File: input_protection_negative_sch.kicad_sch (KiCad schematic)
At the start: 26 parts, among them Q3 SQJQ160E, Q4 SQJQ160E, U2 LM5067

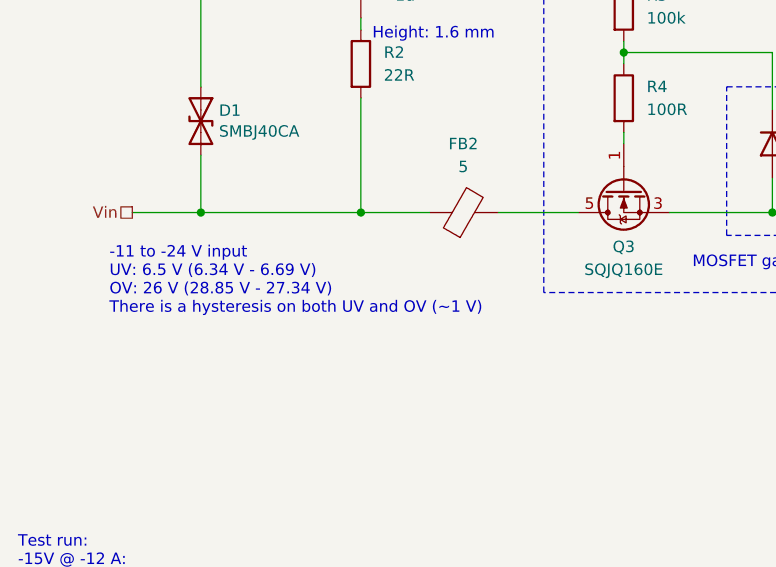
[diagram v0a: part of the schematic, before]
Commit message: Reduced datasheet absolute maximum voltage to ±48 V, because the TVS diodes start conducting considerably at 48 V
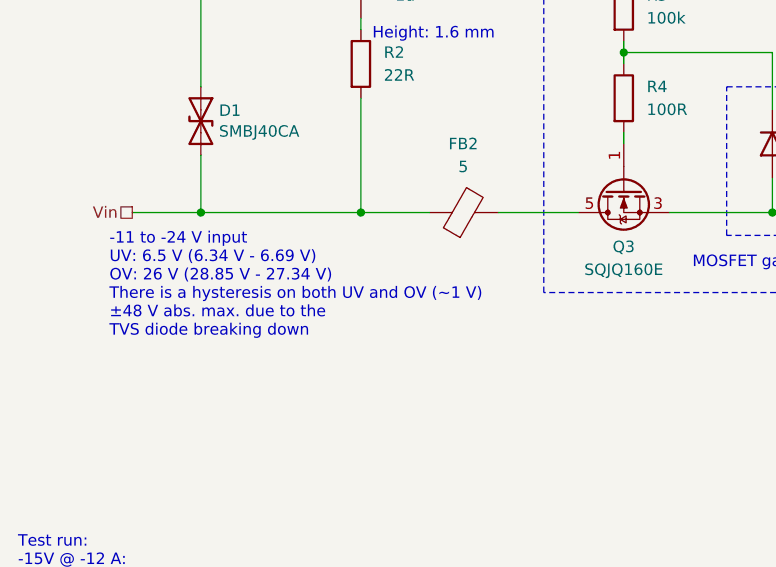
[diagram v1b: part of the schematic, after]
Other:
- note added: "-11 to -24 V input UV: 6.5 V (6.34 V - 6.69 V) OV: 26 V (28.85 V - 27.34 V) There is a hysteresis on both UV and OV (~1 V) ±48 V abs. max. due to the TVS diode breaking down"
- note removed: "-11 to -24 V input UV: 6.5 V (6.34 V - 6.69 V) OV: 26 V (28.85 V - 27.34 V) There is a hysteresis on both UV and OV (~1 V)"
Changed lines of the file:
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@@
     (effects (font (size 1.27 1.27)) (justify left bottom))
   )
-  (text "-11 to -24 V input\nUV: 6.5 V (6.34 V - 6.69 V)\nOV: 26 V (28.85 V - 27.34 V)\nThere is a hysteresis on both UV and OV (~1 V)"
-    (at 36.83 118.11 0)
+  (text "-11 to -24 V input\nUV: 6.5 V (6.34 V - 6.69 V)\nOV: 26 V (28.85 V - 27.34 V)\nThere is a hysteresis on both UV and OV (~1 V)\n±48 V abs. max. due to the\nTVS diode breaking down"
+    (at 36.83 120.65 0)
     (effects (font (size 1.27 1.27)) (justify left bottom))
   )

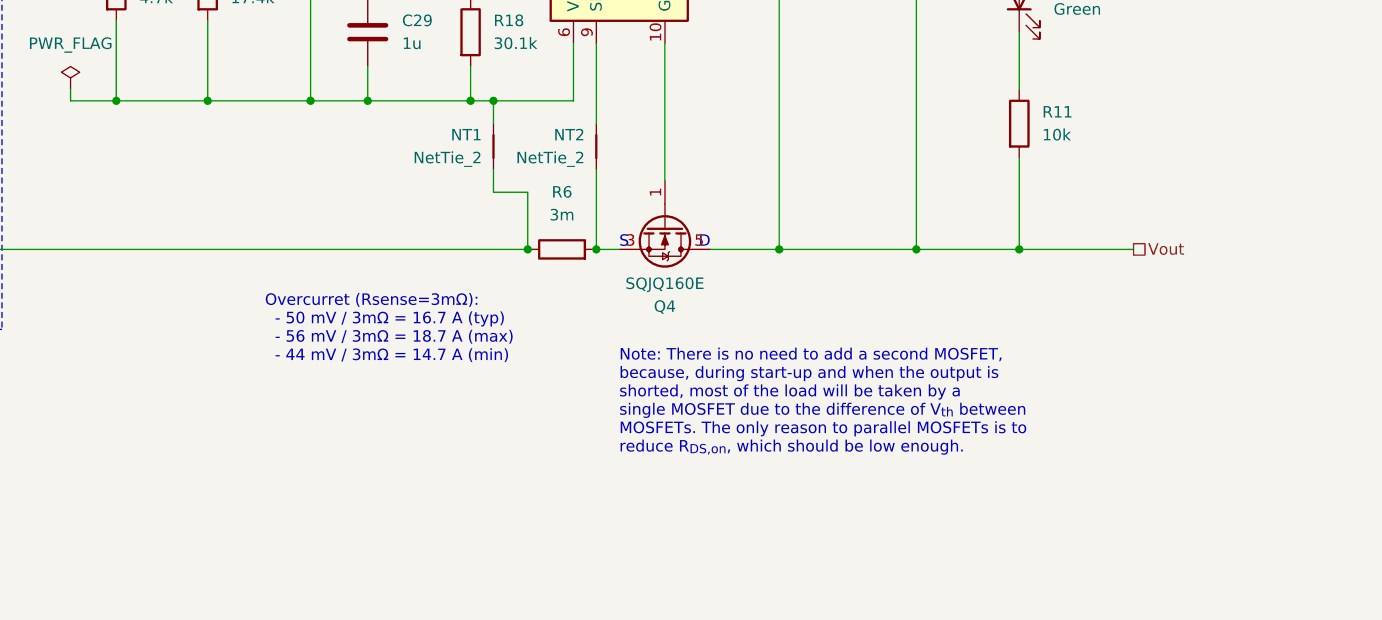
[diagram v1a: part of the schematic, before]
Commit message: Added thermal jumpers Increased copper area at the PMOS and the current sense resistors
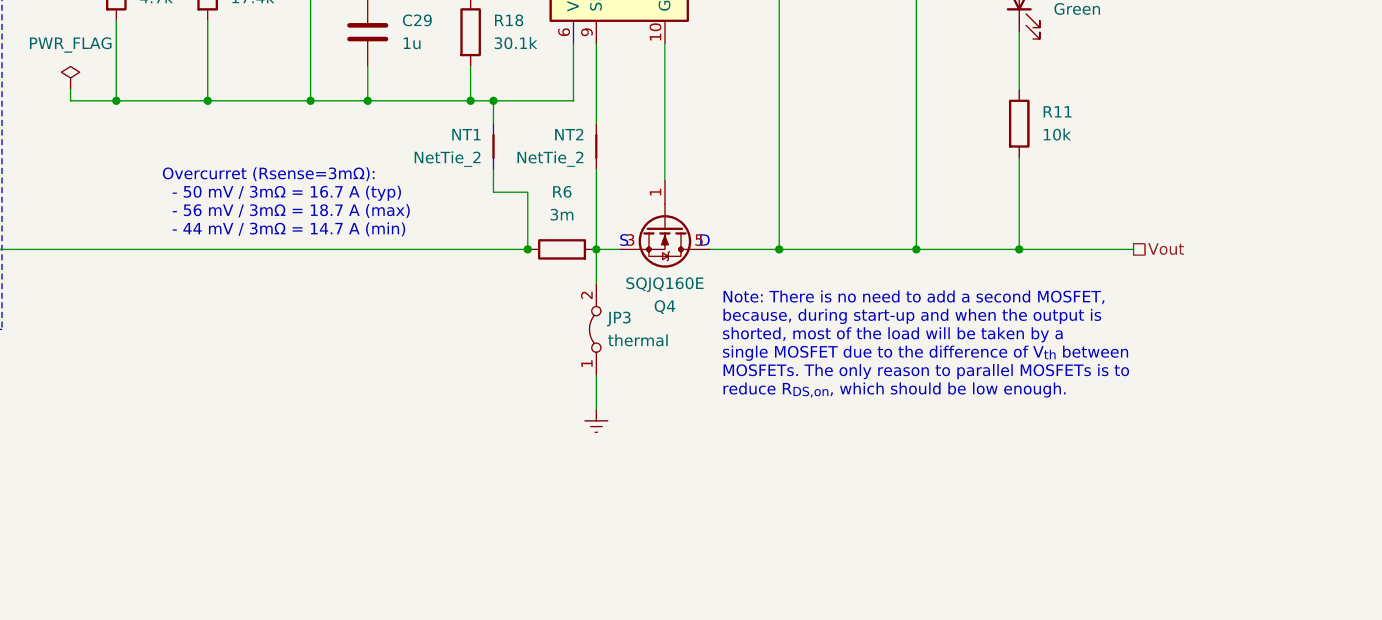
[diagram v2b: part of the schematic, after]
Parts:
- added JP3: thermal, Resistor_SMD:R_0612_1632Metric, symbol Jumper:Jumper_2_Bridged
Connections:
- net at NT2.1, Q4.2 (S), Q4.3 (S)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: now also JP3.2 (B)
- new net Earth: JP3.1 (A)
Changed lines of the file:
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@@
+    (stroke (width 0) (type default))
+  )
+  (wire (pts (xy 205.74 106.68) (xy 205.74 110.49))
     (stroke (width 0) (type default))
   )
@@
   )
   (wire (pts (xy 128.27 39.37) (xy 128.27 85.09))
+    (stroke (width 0) (type default))
+  )
+  (wire (pts (xy 205.74 124.46) (xy 205.74 120.65))
     (stroke (width 0) (type default))
   )
@@
   )
   (text "Note: There is no need to add a second MOSFET,\nbecause, during start-up and when the output is\nshorted, most of the load will be taken by a\nsingle MOSFET due to the difference of V_{th} between\nMOSFETs. The only reason to parallel MOSFETs is to\nreduce R_{DS,on}, which should be low enough."
-    (at 208.28 129.54 0)
+    (at 219.71 123.19 0)
     (effects (font (size 1.27 1.27)) (justify left bottom))
   )
@@
   )
   (text "Overcurret (Rsense=3mΩ):\n  - 50 mV / 3mΩ = 16.7 A (typ)\n  - 56 mV / 3mΩ = 18.7 A (max)\n  - 44 mV / 3mΩ = 14.7 A (min)"
-    (at 168.91 119.38 0)
+    (at 157.48 105.41 0)
     (effects (font (size 1.27 1.27)) (justify left bottom))
   )
@@
     )
   )
+  (symbol (lib_id "power:Earth") (at 205.74 124.46 0) (unit 1)
+    (in_bom yes) (on_board yes) (dnp no) (fields_autoplaced)
+    (property "Reference" "#PWR071" (at 205.74 130.81 0)
+      (effects (font (size 1.27 1.27)) hide)
+    )
+    (property "Value" "Earth" (at 205.74 128.27 0)
+      (effects (font (size 1.27 1.27)) hide)
+    )
+    (property "Footprint" "" (at 205.74 124.46 0)
+      (effects (font (size 1.27 1.27)) hide)
+    )
+    (property "Datasheet" "~" (at 205.74 124.46 0)
+      (effects (font (size 1.27 1.27)) hide)
+    )
+    (pin "1")
+    (instances
+      (project "main"
+        (path "/b4ace06a-3ad4-479e-aaa4-d547ecf6903f/f9160387-088e-4a7b-8d58-b2647e07444c"
+          (reference "#PWR071") (unit 1)
+        )
+        (path "/b4ace06a-3ad4-479e-aaa4-d547ecf6903f/1acfc0a8-4adc-455e-9f2b-420811df0901"
+          (reference "#PWR072") (unit 1)
+        )
+      )
+    )
+  )
   (symbol (lib_id "Device:R") (at 191.77 82.55 0) (unit 1)
     (in_bom yes) (on_board yes) (dnp no) (fields_autoplaced)
@@
         )
       )
+    )
+  )
+  (symbol (lib_id "Jumper:Jumper_2_Bridged") (at 205.74 115.57 90) (unit 1)
+    (in_bom yes) (on_board yes) (dnp no) (fields_autoplaced)
+    (property "Reference" "JP3" (at 207.01 114.3 90)
+      (effects (font (size 1.27 1.27)) (justify right))
+    )
+    (property "Value" "thermal" (at 207.01 116.84 90)
+      (effects (font (size 1.27 1.27)) (justify right))
+    )
+    (property "Footprint" "Resistor_SMD:R_0612_1632Metric" (at 205.74 115.57 0)
+      (effects (font (size 1.27 1.27)) hide)
+    )
+    (property "Datasheet" "~" (at 205.74 115.57 0)
+      (effects (font (size 1.27 1.27)) hide)
+    )
+    (property "MFN" "Vishay" (at 205.74 115.57 0)
+      (effects (font (size 1.27 1.27)) hide)
+    )
+    (property "PN" "THJP0612ABT1" (at 205.74 115.57 0)
+      (effects (font (size 1.27 1.27)) hide)
+    )
+    (pin "2")
+    (pin "1")
+    (instances
+      (project "main"
+        (path "/b4ace06a-3ad4-479e-aaa4-d547ecf6903f/f9160387-088e-4a7b-8d58-b2647e07444c"
+          (reference "JP3") (unit 1)
+        )
+        (path "/b4ace06a-3ad4-479e-aaa4-d547ecf6903f/1acfc0a8-4adc-455e-9f2b-420811df0901"
+          (reference "JP4") (unit 1)
+        )
+      )

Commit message: Updated RoHS information
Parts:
- D6: RoHS (none) -> Yes; Temperature (none) -> Tstorage = –40 °C to 150 °C
- JP3: PN THJP0612ABT1 -> THJP0612AST1; RoHS (none) -> Yes; Temperature (none) -> Tstorage = –65 °C to 150 °C
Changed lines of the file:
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@@
       (effects (font (size 1.27 1.27)) hide)
     )
-    (property "PN" "THJP0612ABT1" (at 205.74 115.57 0)
+    (property "PN" "THJP0612AST1" (at 205.74 115.57 0)
+      (effects (font (size 1.27 1.27)) hide)
+    )
+    (property "RoHS" "Yes" (at 205.74 115.57 0)
+      (effects (font (size 1.27 1.27)) hide)
+    )
+    (property "Temperature" "Tstorage = –65 °C to 150 °C" (at 205.74 115.57 0)
       (effects (font (size 1.27 1.27)) hide)
     )
@@
       (effects (font (size 1.27 1.27)) hide)
     )
+    (property "RoHS" "Yes" (at 208.28 45.72 0)
+      (effects (font (size 1.27 1.27)) hide)
+    )
+    (property "Temperature" "Tstorage = –40 °C to 150 °C" (at 208.28 45.72 0)
+      (effects (font (size 1.27 1.27)) hide)
+    )

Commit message: Added test points
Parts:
- added TP3: TestPoint, TestPoint:TestPoint_Pad_D1.5mm, symbol Connector:TestPoint
- renumbered D6 to D4, R15 to R14, R16 to R15, R17 to R16, R18 to R17
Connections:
- net at FB2.2, Q3.5 (D): now also TP3.1
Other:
- moved on the sheet: C22, C24, C29, D4, D7, D8, JP3, NT1, NT2, Q3, Q4, R11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

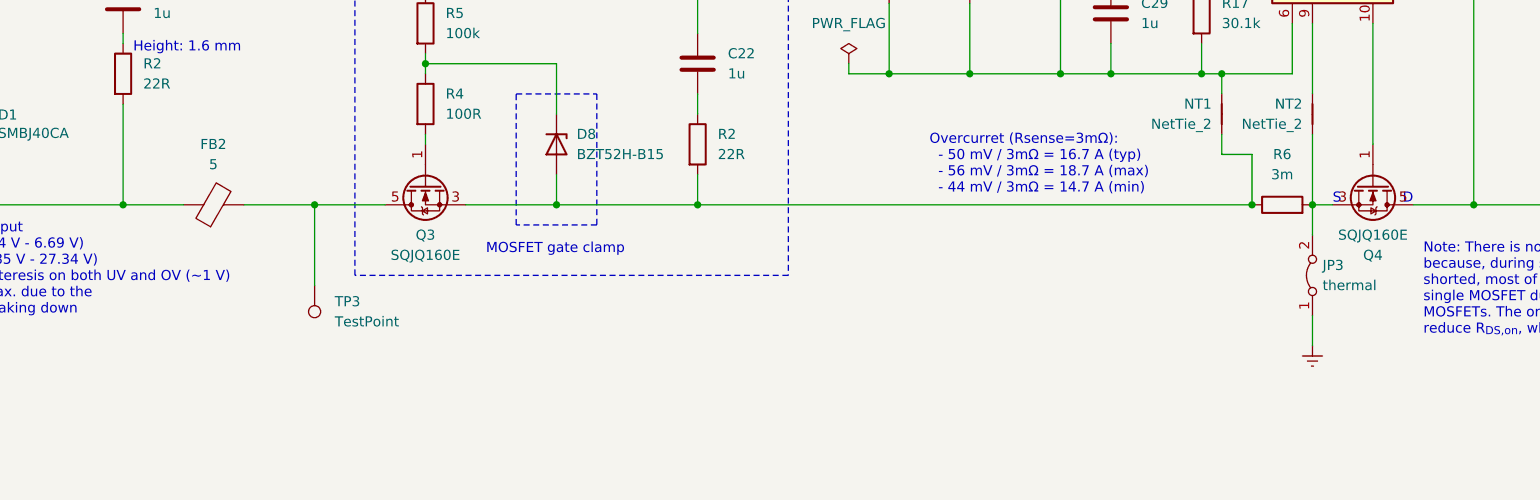
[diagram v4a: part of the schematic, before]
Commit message: Cleaned up BOM
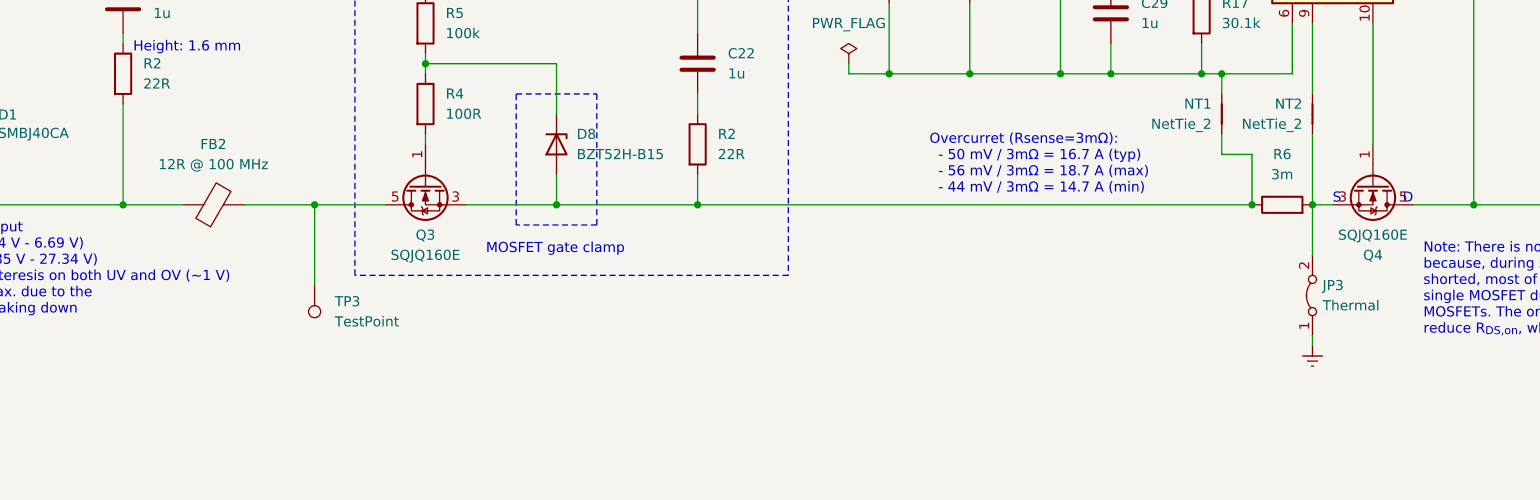
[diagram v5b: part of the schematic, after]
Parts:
- FB2: value 5 -> 12R @ 100 MHz
- JP3: value thermal -> Thermal
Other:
- moved on the sheet: JP3
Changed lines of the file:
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@@
     (stroke (width 0) (type default))
   )
-  (wire (pts (xy 214.63 106.68) (xy 214.63 110.49))
+  (wire (pts (xy 214.63 106.68) (xy 214.63 113.03))
     (stroke (width 0) (type default))
   )
@@
     (stroke (width 0) (type default))
   )
-  (wire (pts (xy 214.63 124.46) (xy 214.63 120.65))
+  (wire (pts (xy 214.63 124.46) (xy 214.63 123.19))
     (stroke (width 0) (type default))
   )
@@
       (effects (font (size 1.27 1.27)))
     )
-    (property "Value" "5" (at 76.1492 101.6 90)
+    (property "Value" "12R @ 100 MHz" (at 76.1492 101.6 90)
       (effects (font (size 1.27 1.27)))
     )
@@
     )
   )
-  (symbol (lib_id "Jumper:Jumper_2_Bridged") (at 214.63 115.57 90) (unit 1)
-    (in_bom yes) (on_board yes) (dnp no) (fields_autoplaced)
-    (property "Reference" "JP3" (at 215.9 114.3 90)
+  (symbol (lib_id "Jumper:Jumper_2_Bridged") (at 214.63 118.11 90) (unit 1)
+    (in_bom yes) (on_board yes) (dnp no) (fields_autoplaced)
+    (property "Reference" "JP3" (at 215.9 116.84 90)
       (effects (font (size 1.27 1.27)) (justify right))
     )
-    (property "Value" "thermal" (at 215.9 116.84 90)
+    (property "Value" "Thermal" (at 215.9 119.38 90)
       (effects (font (size 1.27 1.27)) (justify right))
     )
-    (property "Footprint" "Resistor_SMD:R_0612_1632Metric" (at 214.63 115.57 0)
-      (effects (font (size 1.27 1.27)) hide)
-    )
-    (property "Datasheet" "~" (at 214.63 115.57 0)
-      (effects (font (size 1.27 1.27)) hide)
-    )
-    (property "MFN" "Vishay" (at 214.63 115.57 0)
-      (effects (font (size 1.27 1.27)) hide)
-    )
-    (property "PN" "THJP0612AST1" (at 214.63 115.57 0)
-      (effects (font (size 1.27 1.27)) hide)
-    )
-    (property "RoHS" "Yes" (at 214.63 115.57 0)
-      (effects (font (size 1.27 1.27)) hide)
-    )
-    (property "Temperature" "Tstorage = –65 °C to 150 °C" (at 214.63 115.57 0)
-      (effects (font (size 1.27 1.27)) hide)
-    )
+    (property "Footprint" "Resistor_SMD:R_0612_1632Metric" (at 214.63 118.11 0)
+      (effects (font (size 1.27 1.27)) hide)
+    )
+    (property "Datasheet" "~" (at 214.63 118.11 0)
+      (effects (font (size 1.27 1.27)) hide)
+    )
+    (property "MFN" "Vishay" (at 214.63 118.11 0)
+      (effects (font (size 1.27 1.27)) hide)
+    )
+    (property "PN" "THJP0612AST1" (at 214.63 118.11 0)
+      (effects (font (size 1.27 1.27)) hide)
+    )
+    (property "RoHS" "Yes" (at 214.63 118.11 0)
+      (effects (font (size 1.27 1.27)) hide)
+    )
+    (property "Temperature" "Tstorage = –65 °C to 150 °C" (at 214.63 118.11 0)
+      (effects (font (size 1.27 1.27)) hide)
+    )
